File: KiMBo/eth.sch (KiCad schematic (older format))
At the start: 45 parts, among them U12 LAN8710A, U2 OSD3358, Y1 CRYSTAL

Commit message: Begin entry of component values
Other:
- note added: "VDD_3V3B is the source"
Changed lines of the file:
@@
 	6850 2400 6850 2450
 Connection ~ 6850 2450
+Text Notes 6550 1250 0    60   ~ 0
+VDD_3V3B is the source
 $EndSCHEMATC

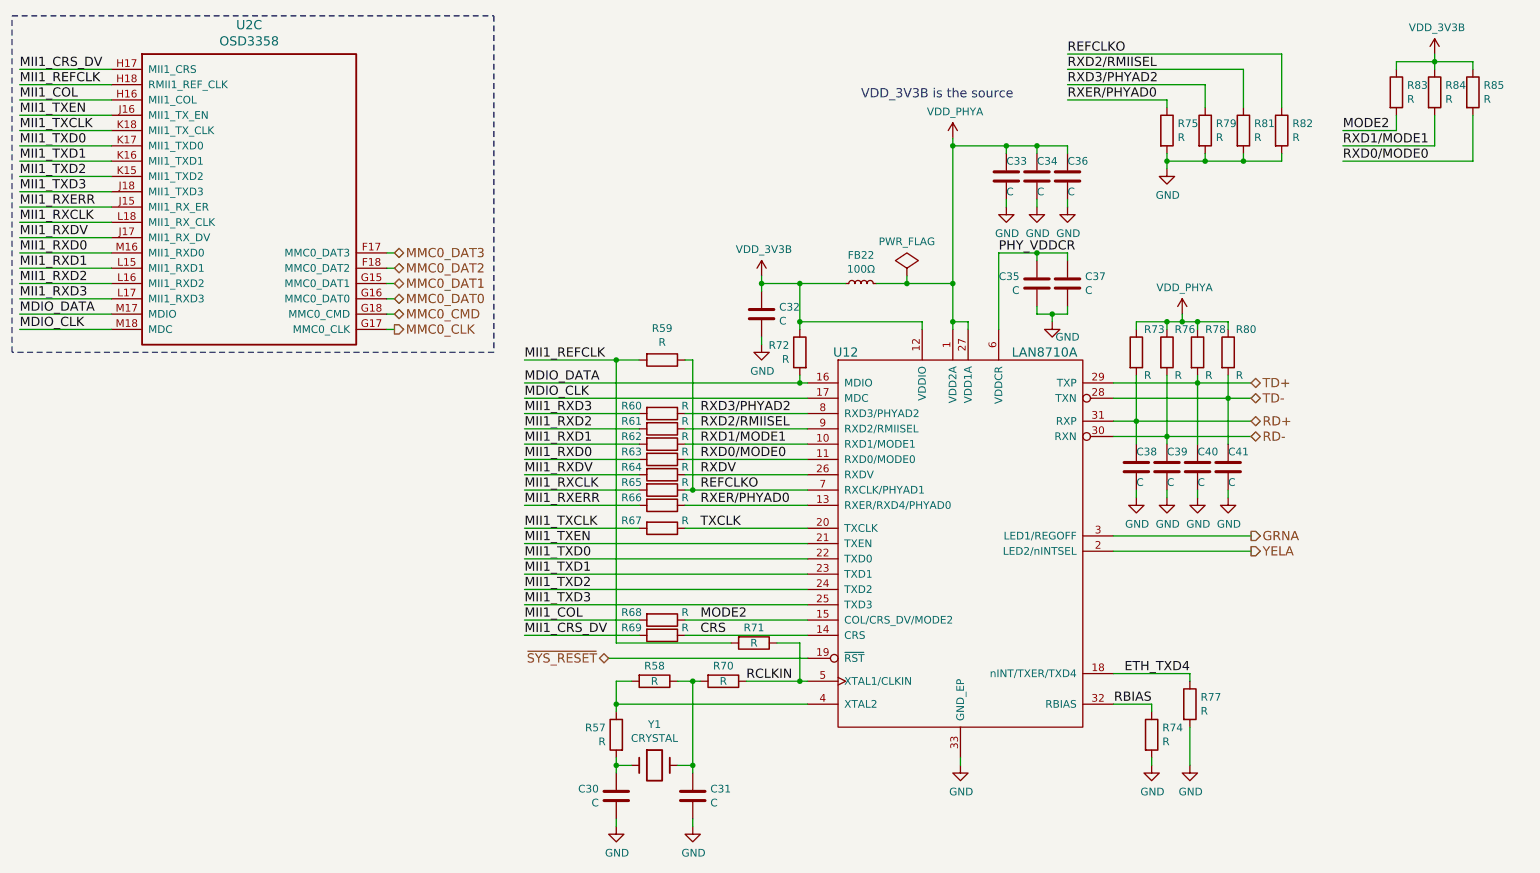
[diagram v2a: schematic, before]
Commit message: Entry of additional component values
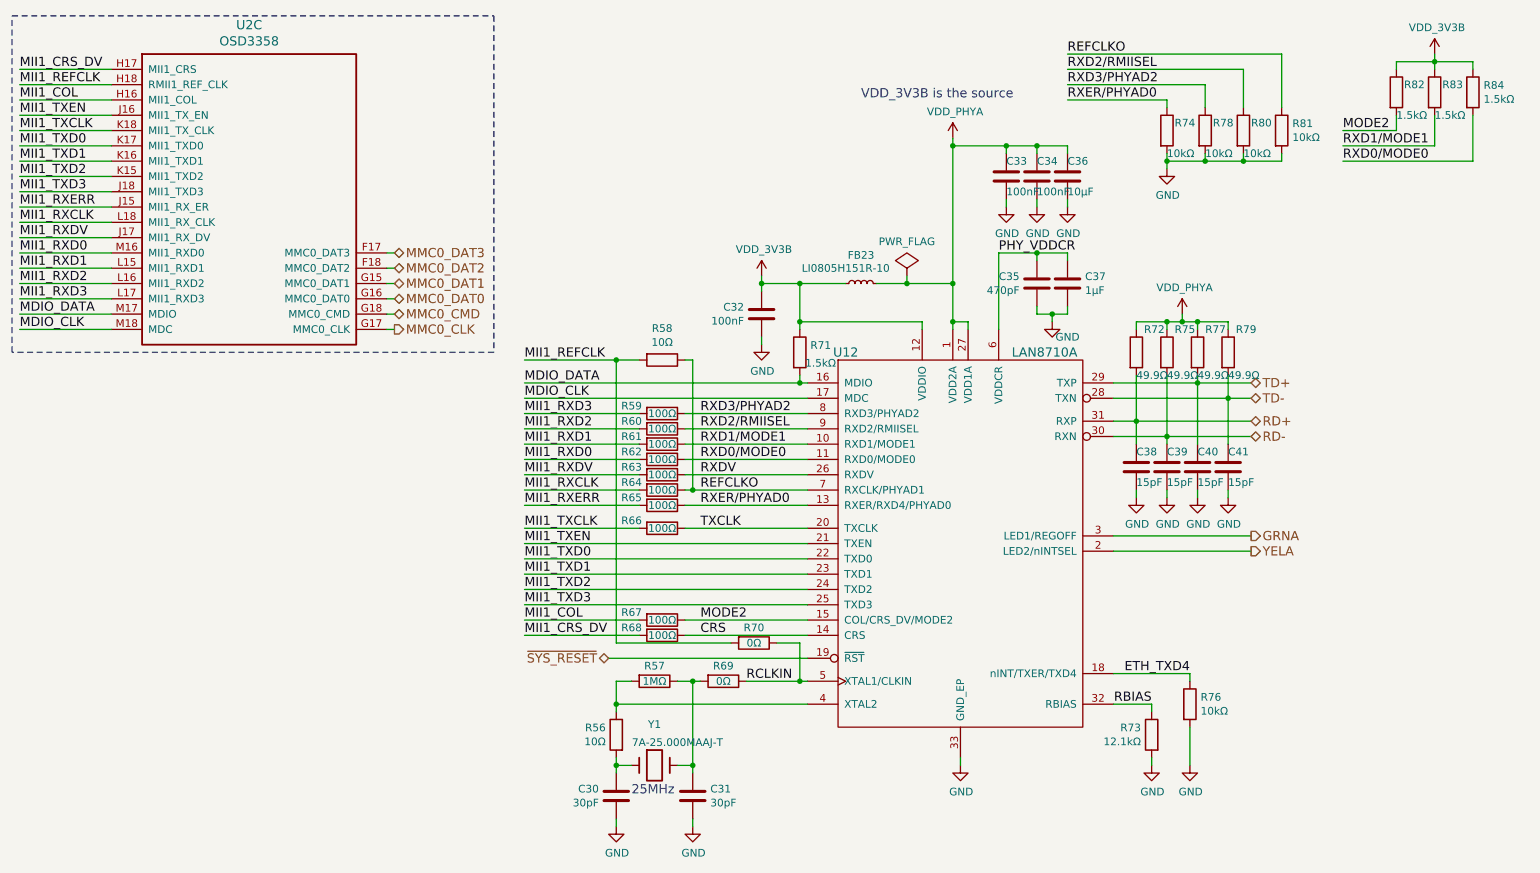
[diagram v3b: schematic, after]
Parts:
- C30, C31: value C -> 30pF
- C32, C33, C34: value C -> 100nF
- C35: value C -> 470pF
- C36: value C -> 10μF
- C37: value C -> 1μF
- C38, C39, C40, C41: value C -> 15pF
- FB23: renamed from FB22; value 100Ω -> LI0805H151R-10
- R56: renamed from R57; value R -> 10Ω
- R57: renamed from R58; value R -> 1MΩ
- R58: renamed from R59; value R -> 10Ω
- R59: renamed from R60; value R -> 100Ω
- R60: renamed from R61; value R -> 100Ω
- R61: renamed from R62; value R -> 100Ω
- R62: renamed from R63; value R -> 100Ω
- R63: renamed from R64; value R -> 100Ω
- R64: renamed from R65; value R -> 100Ω
- R65: renamed from R66; value R -> 100Ω
- R66: renamed from R67; value R -> 100Ω
- R67: renamed from R68; value R -> 100Ω
- R68: renamed from R69; value R -> 100Ω
- R69: renamed from R70; value R -> 0Ω
- R70: renamed from R71; value R -> 0Ω
- R71: renamed from R72; value R -> 1.5kΩ
- R72: renamed from R73; value R -> 49.9Ω
- R73: renamed from R74; value R -> 12.1kΩ
- R74: renamed from R75; value R -> 10kΩ
- R75: renamed from R76; value R -> 49.9Ω
- R76: renamed from R77; value R -> 10kΩ
- R77: renamed from R78; value R -> 49.9Ω
- R78: renamed from R79; value R -> 10kΩ
- R79: renamed from R80; value R -> 49.9Ω
- R80: renamed from R81; value R -> 10kΩ
- R81: renamed from R82; value R -> 10kΩ
- R82: renamed from R83; value R -> 1.5kΩ
- R83: renamed from R84; value R -> 1.5kΩ
- R84: renamed from R85; value R -> 1.5kΩ
- Y1: value CRYSTAL -> 7A-25.000MAAJ-T
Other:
- note added: "25MHz"

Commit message: Add equivalent annotations document, associate more footprints
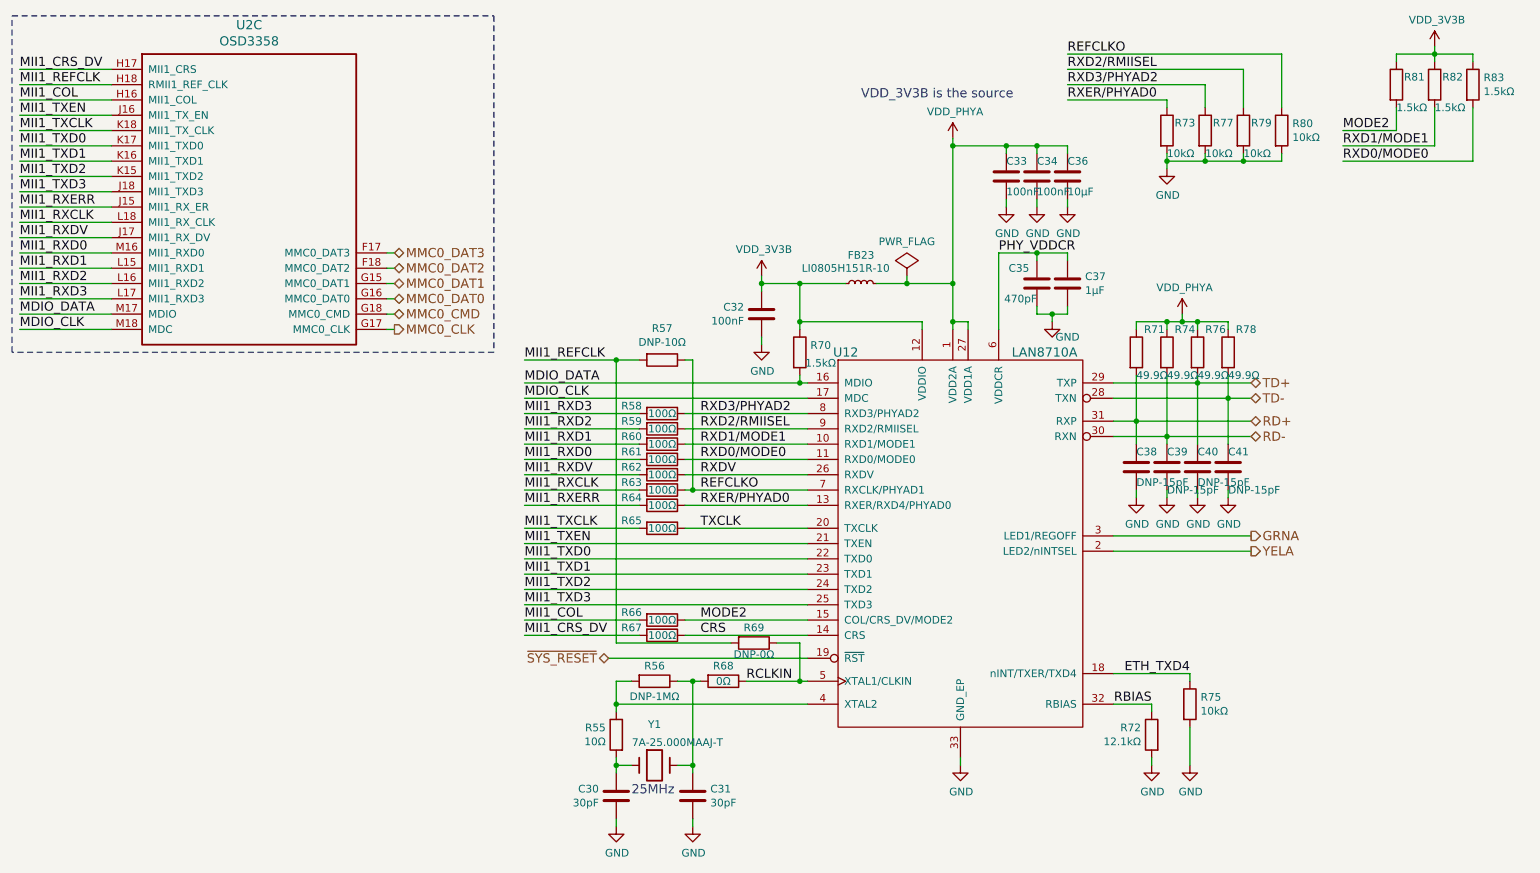
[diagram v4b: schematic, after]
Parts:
- C30, C31, C32, C33, C34, C35, C37: footprint (none) -> Capacitors_SMD:C_0402
- C36: footprint (none) -> Capacitors_SMD:C_0805
- C38, C39, C40, C41: value 15pF -> DNP-15pF; footprint (none) -> Capacitors_SMD:C_0402
- R55: renamed from R56; footprint (none) -> Resistors_SMD:R_0402
- R56: renamed from R57; value 1MΩ -> DNP-1MΩ
- R57: renamed from R58; value 10Ω -> DNP-10Ω
- R58: renamed from R59; footprint (none) -> Resistors_SMD:R_0402
- R59: renamed from R60; footprint (none) -> Resistors_SMD:R_0402
- R60: renamed from R61; footprint (none) -> Resistors_SMD:R_0402
- R61: renamed from R62; footprint (none) -> Resistors_SMD:R_0402
- R62: renamed from R63; footprint (none) -> Resistors_SMD:R_0402
- R63: renamed from R64; footprint (none) -> Resistors_SMD:R_0402
- R64: renamed from R65; footprint (none) -> Resistors_SMD:R_0402
- R65: renamed from R66; footprint (none) -> Resistors_SMD:R_0402
- R66: renamed from R67; footprint (none) -> Resistors_SMD:R_0402
- R67: renamed from R68; footprint (none) -> Resistors_SMD:R_0402
- R68: renamed from R69; footprint (none) -> Resistors_SMD:R_0402
- R69: renamed from R70; value 0Ω -> DNP-0Ω; footprint (none) -> Resistors_SMD:R_0402
- R70: renamed from R71; footprint (none) -> Resistors_SMD:R_0402
- R71: renamed from R72; footprint (none) -> Resistors_SMD:R_0402
- R72: renamed from R73; footprint (none) -> Resistors_SMD:R_0402
- R73: renamed from R74; footprint (none) -> Resistors_SMD:R_0402
- R74: renamed from R75; footprint (none) -> Resistors_SMD:R_0402
- R75: renamed from R76; footprint (none) -> Resistors_SMD:R_0402
- R76: renamed from R77; footprint (none) -> Resistors_SMD:R_0402
- R77: renamed from R78; footprint (none) -> Resistors_SMD:R_0402
- R78: renamed from R79; footprint (none) -> Resistors_SMD:R_0402
- R79: renamed from R80; footprint (none) -> Resistors_SMD:R_0402
- R80: renamed from R81; footprint (none) -> Resistors_SMD:R_0402
- R81: renamed from R82; footprint (none) -> Resistors_SMD:R_0402
- R82: renamed from R83; footprint (none) -> Resistors_SMD:R_0402
- R83: renamed from R84; footprint (none) -> Resistors_SMD:R_0402
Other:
- moved on the sheet: R81, R82, R83

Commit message: Leave SPI0 free for a display, reassign pins so SPI1 is available
Fix some typos/errors
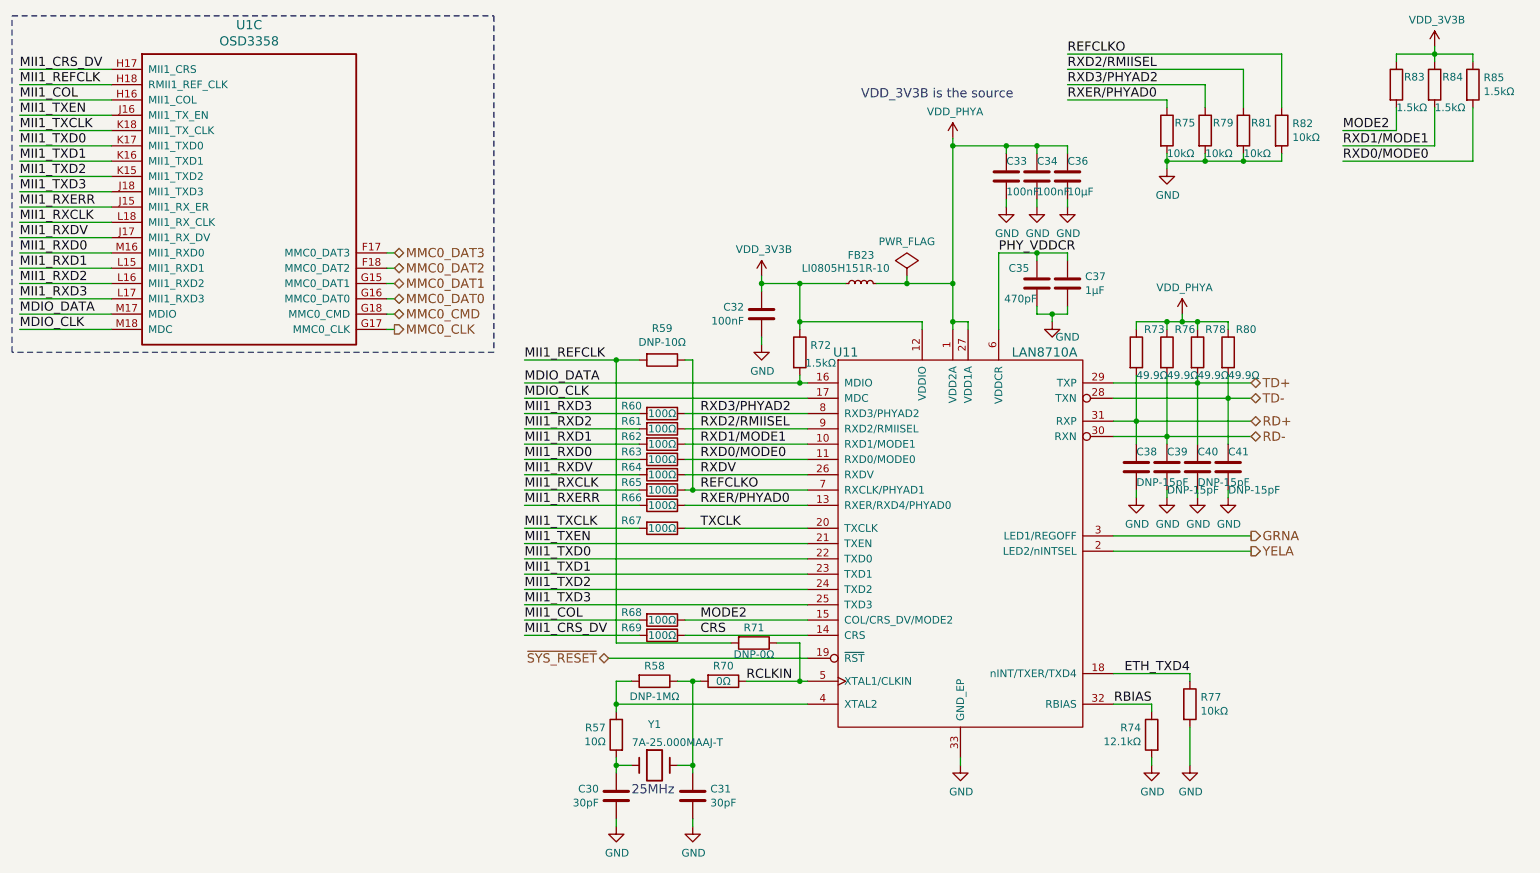
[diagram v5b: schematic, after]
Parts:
- renumbered R55 to R57, R56 to R58, R57 to R59, R58 to R60, R59 to R61, R60 to R62, R61 to R63, R62 to R64, R63 to R65, R64 to R66, R65 to R67, R66 to R68, R67 to R69, R68 to R70, R69 to R71, R70 to R72, R71 to R73, R72 to R74, R73 to R75, R74 to R76, R75 to R77, R76 to R78, R77 to R79, R78 to R80, R79 to R81, R80 to R82, R81 to R83, R82 to R84, R83 to R85, U2 to U1, U12 to U11

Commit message: Use fixed 5V LM2592HV Buck, include SPI0 header for LCD
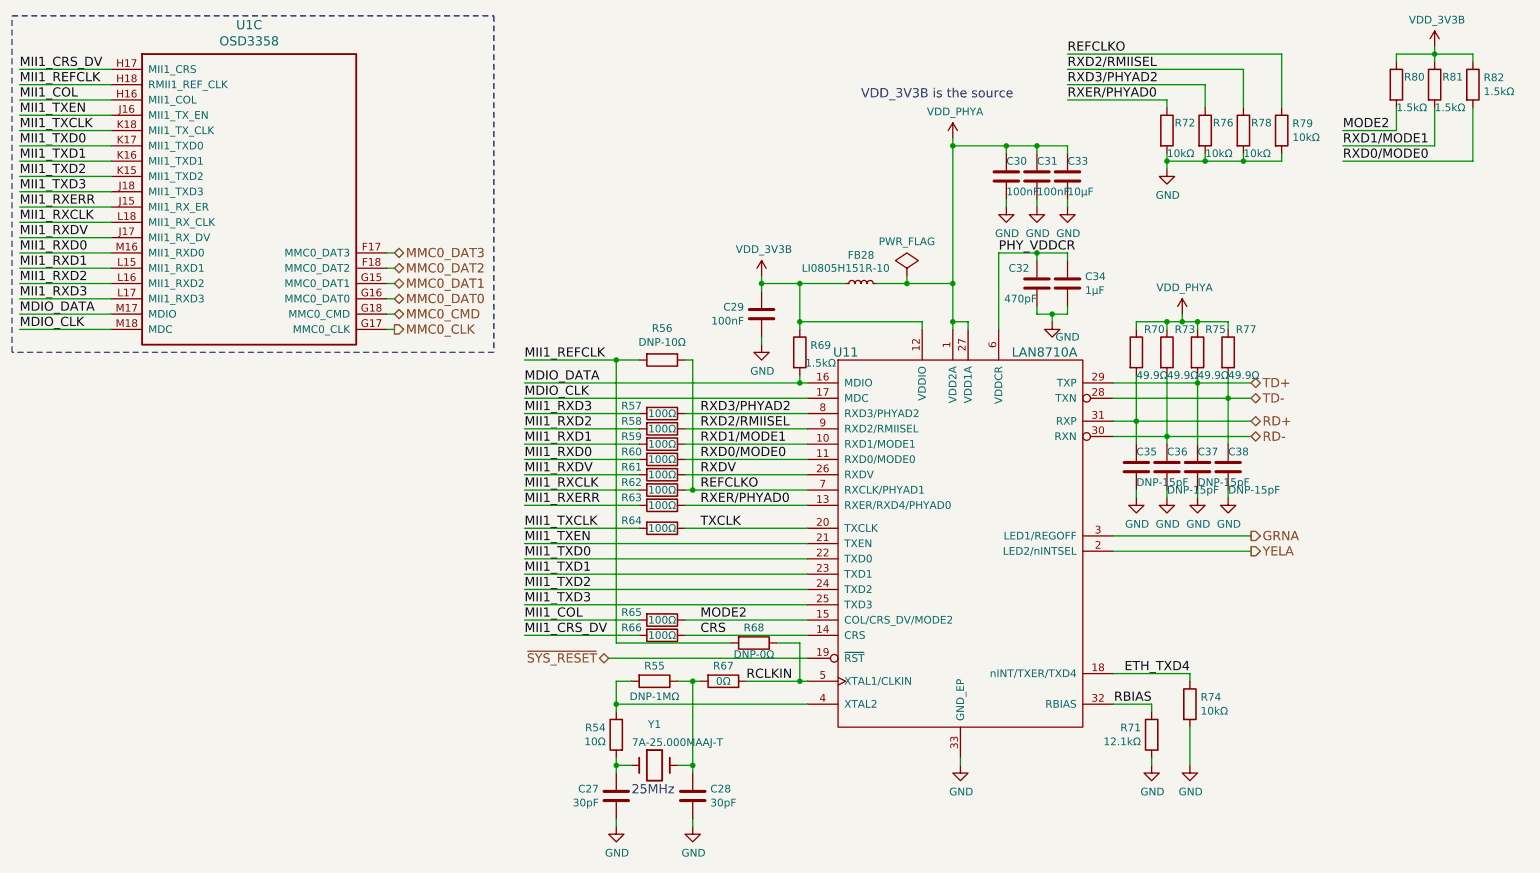
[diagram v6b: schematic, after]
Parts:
- renumbered C30 to C27, C31 to C28, C32 to C29, C33 to C30, C34 to C31, C35 to C32, C36 to C33, C37 to C34, C38 to C35, C39 to C36, C40 to C37, C41 to C38, FB23 to FB28, R57 to R54, R58 to R55, R59 to R56, R60 to R57, R61 to R58, R62 to R59, R63 to R60, R64 to R61, R65 to R62, R66 to R63, R67 to R64, R68 to R65, R69 to R66, R70 to R67, R71 to R68, R72 to R69, R73 to R70, R74 to R71, R75 to R72, R76 to R73, R77 to R74, R78 to R75, R79 to R76, R80 to R77, R81 to R78, R82 to R79, R83 to R80, R84 to R81, R85 to R82
